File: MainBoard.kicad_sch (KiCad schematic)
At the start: 48 parts, among them SW1 SW_Push, SW10 SW_Push, SW11 SW_Push, SW12 SW_Push, SW13 SW_Push, SW14 SW_Push, SW15 SW_Push, SW16 SW_Push, SW17 SW_Push, SW18 SW_Push, SW19 SW_Push, SW2 SW_Push, SW20 SW_Push, SW21 SW_Push, SW22 SW_Push, SW23 SW_Push, SW3 SW_Push, SW4 SW_Push, SW5 SW_Push, SW6 SW_Push, SW7 SW_Push, SW8 SW_Push, SW9 SW_Push

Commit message: added PCB connectors
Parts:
- removed BZ1, BZ2: Buzzer, symbol Device:Buzzer
- removed D1, D10, D11, D2, D6, D7, D8, D9, docD5: LED, symbol Device:LED
- removed RV1, RV2: R_Potentiometer, symbol Device:R_Potentiometer
- removed SW1, SW11, SW12, SW13, SW14, SW15, SW16, SW17, SW2, SW3, SW4, SW5, SW6, SW7: SW_Push, symbol Switch:SW_Push
- added J1, J17, J18, J19: (no value), symbol higo:Z209BM_C_04_00_0000
- added J10, J23: (no value), symbol JST_JWPF:B03B-JWPF-SK-R
- added J11, J22: (no value), symbol JST_JWPF:B04B-JWPF-SK-R
- added J12: Conn_01x02, symbol Connector_Generic:Conn_01x02
- added J13: Conn_01x06, symbol Connector_Generic:Conn_01x06
- added J14, J16: Conn_01x09, symbol Connector_Generic:Conn_01x09
- added J2, J20: (no value), symbol higo:Z309BM_C_04_00_0000
- added J21: (no value), symbol JST_JWPF:B05B-JWPF-SK-R
- added J3: (no value), symbol higo:Z409BM_C_04_00_0000
- added J5: (no value), symbol higo:Z509BM_C_04_00_0000
- added J6: (no value), symbol higo:Z609BM_C_04_00_0000
- added J8: (no value), symbol higo:Z809FM_C_04_00_0000
- added J9: (no value), symbol JST_JWPF:B02B-JWPF-SK-R
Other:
- note added: "PAS"
- note added: "accelerator"
- note added: "brake left"
- note added: "brake right"
- note added: "front connector"
- note added: "left side blinker"
- note added: "lightning commodo"
- note added: "motor commodo"
- note added: "right side blinker"
- note added: "seat switch"
- note added: "tail connector"
- note added: "torque"
- note added: "trunk light"
- note added: "trunk switch"
- note removed: "7 Output Digital Rear 7 analog input Rear 6/7 Output Digital Front 6/7 analog input Front 5 analog IN HMI 20 digital input 4 digital output"
- note removed: "Assist + Assist - Reverse Forward speed limiter setpoint warning on/off ? GND"
- note removed: "Beware, different GND..."
- note removed: "Blinker Left Blinker Left Sequential Reverse light VCC T2 Brake T2 Fog light Blinker Right Blinker Right Sequential GND"
- note removed: "Blinker Left Side Light Left VCC E6C SW+ E6C SW- E6C Side Light Right Blinker Right Horn GND"
- note removed: "BrightstarTW A1 Vcc Blink GND"
- note removed: "BrightstarTW E6C Vcc (DRL) SW (shorting the sw SW wire switch between GND the mode DRL -> PASSING <-> DRIVING )"
- note removed: "BrightstarTW T2 Vcc (license plate + Pos) brake Vcc GND"
- note removed: "DK370"
- note removed: "PAS Front"
- note removed: "Speed limiter -> Mode switch, Assist <-> Speed limtier ?"
- note removed: "Throttle"
- note removed: "Torque rear"
- note removed: "VCC GND S1 S2 Torque"
- note removed: "VDS blinker + beam tell tale"
- note removed: "beam horn blinker L blinker R GND"
- note removed: "bonus for speed limiter"
- note removed: "https://ebikes.ca/resources/theory/pedal-assist.html"
- note removed: "left brake"
- note removed: "pedal regen"
- note removed: "right brake"
- note removed: "seat sensor"

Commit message: added output driver
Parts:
- removed SW10, SW18, SW19, SW20, SW21, SW22, SW23, SW8, SW9: SW_Push, symbol Switch:SW_Push
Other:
- sheet FrontLightsControl renamed outputdriver
- sheet HumanInterfaceCircuits renamed inputHMI
- removed sheet BMSinterface
- removed sheet BackLightsControl
- added sheet IMU (USB_PD.kicad_sch)
- sheet outputdriver ports: added Load0, Load1, Load10, Load11, Load12, Load13, Load14, Load15, Load16, Load17, Load18, Load19, Load2, Load3, Load4, Load5, Load6, Load7, Load8, Load9; removed none
- note added: "DONT FORGET : IMU foglight feedback buzzer"
- note added: "tell tale VDS"
- moved on the sheet: FID1, FID2, FID3, FID4, FID5, FID6, H1, H2, H3, H4, H5, H6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

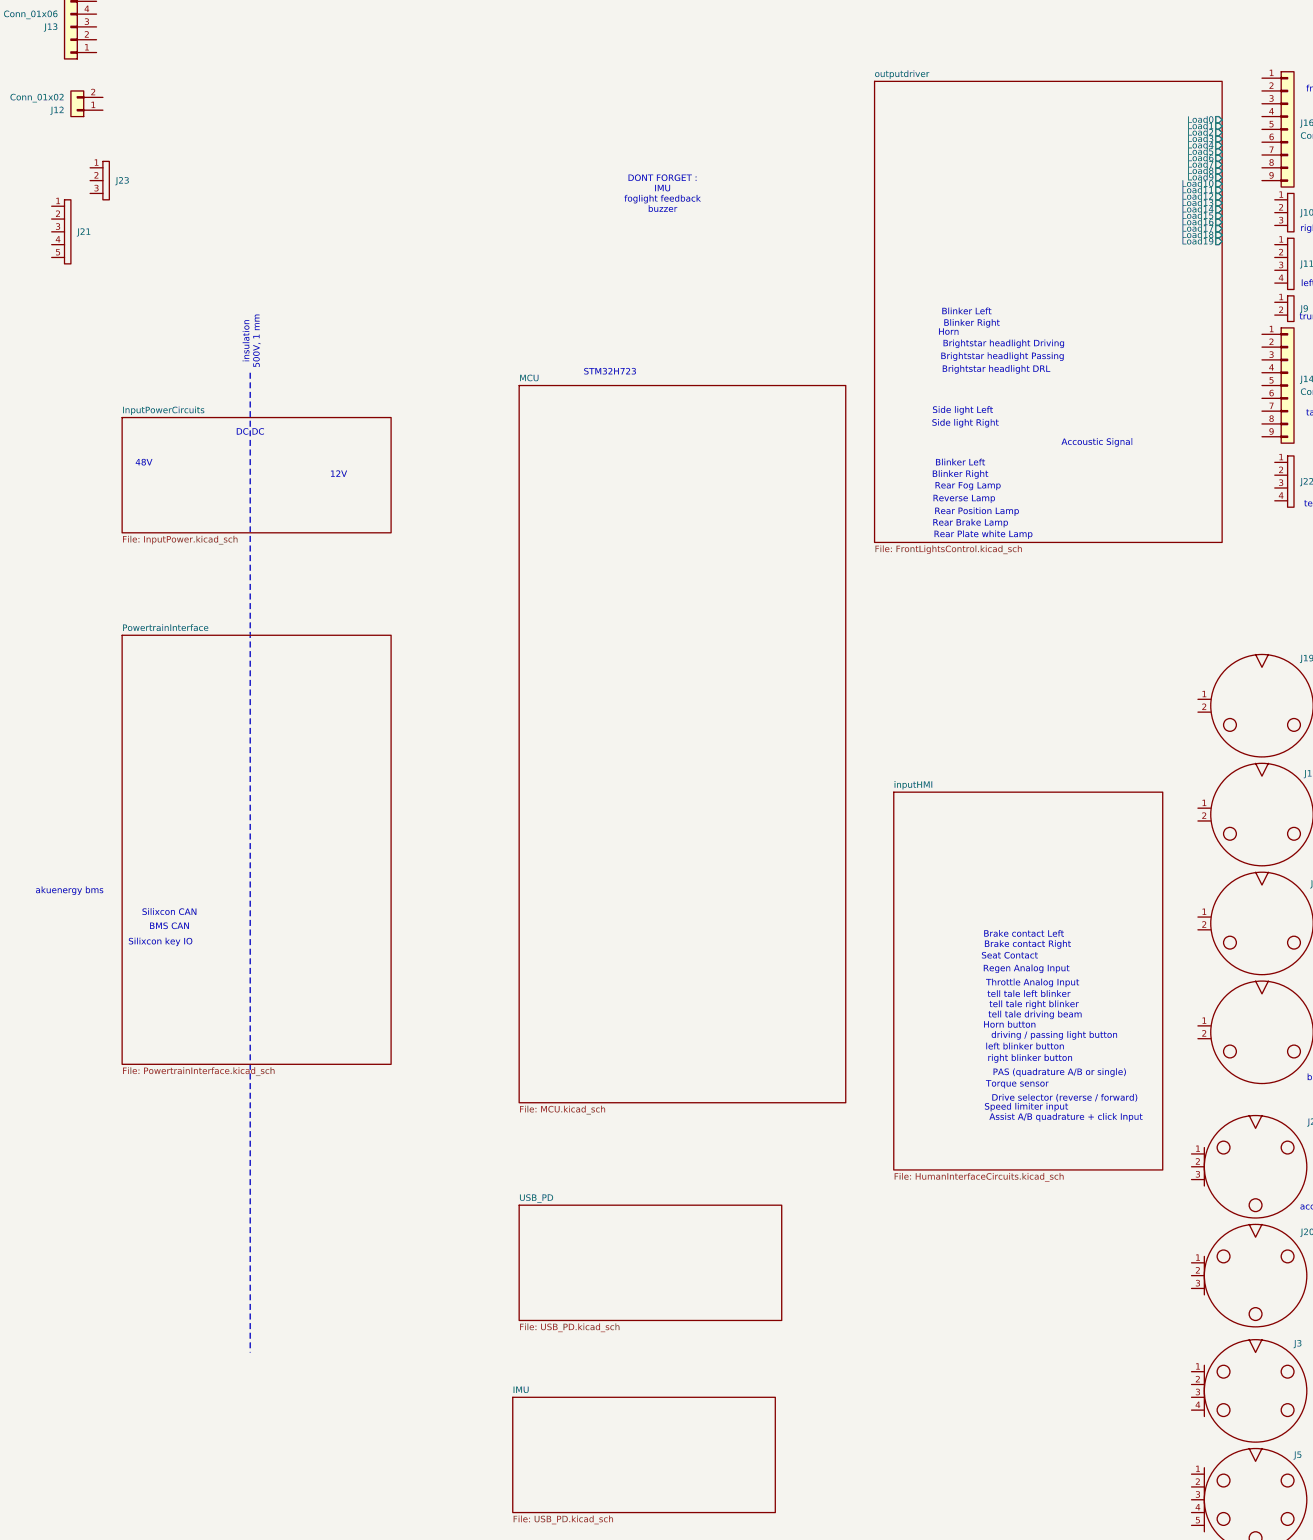
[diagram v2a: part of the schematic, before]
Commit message: added schematic for input (switch, PAS, analog) + output
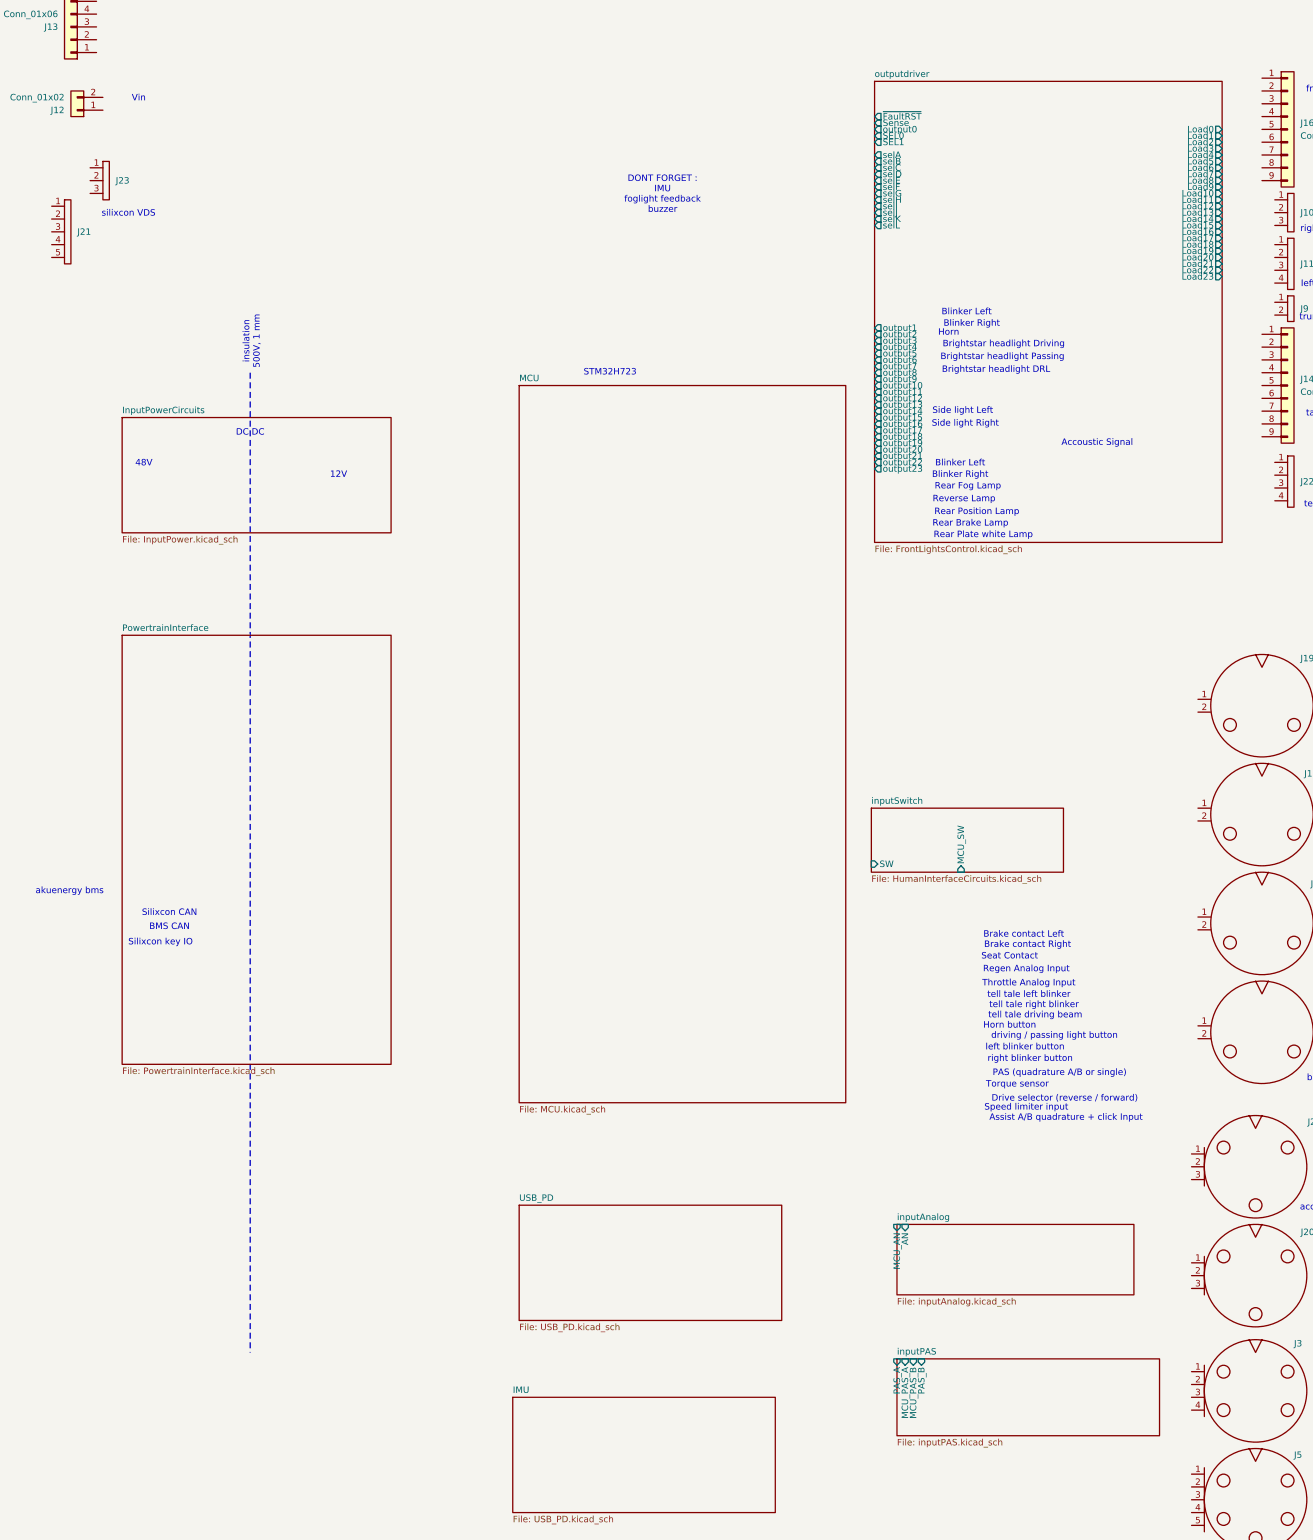
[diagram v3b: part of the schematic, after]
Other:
- sheet inputHMI renamed inputSwitch
- added sheet inputAnalog (inputAnalog.kicad_sch)
- added sheet inputPAS (inputPAS.kicad_sch)
- sheet inputSwitch ports: added MCU_SW, SW; removed none
- sheet outputdriver ports: added Load20, Load21, Load22, Load23, SEL0, SEL1, Sense, output0, output1, output10, output11, output12, output13, output14, output15, output16, output17, output18, output19, output2, output20, output21, output22, output23, output3, output4, output5, output6, output7, output8, output9, selA, selB, selC, selD, selE, selF, selG, selH, selI, selJ, selK, selL, ~{FaultRST}; removed none
- note added: "Vin"
- note added: "silixcon VDS"

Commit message: wiring MCU to input and ouput
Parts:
- added J25: (no value), symbol higo:Z609BM_C_04_00_0000
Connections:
- net inputAnalog/AN: now also J20.3
- net inputPAS/PAS_A: now also J6.4
- net inputPAS/PAS_B: now also J6.3
- net inputSwitch/SW: now also J19.2
- net outputdriver/Load0: now also J16.2 (Pin_2)
- net outputdriver/Load1: now also J16.3 (Pin_3)
- net outputdriver/Load10: now also J11.2
- net outputdriver/Load11: now also J11.3
- net outputdriver/Load12: now also J9.2
- net outputdriver/Load13: now also J14.2 (Pin_2)
- net outputdriver/Load14: now also J14.3 (Pin_3)
- net outputdriver/Load15: now also J14.4 (Pin_4)
- net outputdriver/Load16: now also J14.5 (Pin_5)
- net outputdriver/Load17: now also J14.6 (Pin_6)
- net outputdriver/Load18: now also J14.7 (Pin_7)
- net outputdriver/Load19: now also J14.8 (Pin_8)
- net outputdriver/Load2: now also J16.4 (Pin_4)
- net outputdriver/Load20: now also J14.9 (Pin_9)
- net outputdriver/Load21: now also J22.1
- net outputdriver/Load22: now also J22.2
- net outputdriver/Load23: now also J22.3
- net outputdriver/Load3: now also J16.5 (Pin_5)
- net outputdriver/Load4: now also J16.6 (Pin_6)
- net outputdriver/Load5: now also J16.7 (Pin_7)
- net outputdriver/Load6: now also J16.8 (Pin_8)
- net outputdriver/Load7: now also J16.9 (Pin_9)
- net outputdriver/Load8: now also J10.2
- net outputdriver/Load9: now also J10.3
- net GND: now reaches J5.1
- net GND: now also J1.1, J10.1, J11.1, J14.1 (Pin_1), J16.1 (Pin_1), J17.1, J18.1, J19.1, J2.2, J20.2, J22.4, J3.2, J6.2, J8.1, J9.1, J25.2
- net inputSwitch4/SW: now reaches J5.2
- net inputSwitch5/SW: now reaches J5.3
- net inputSwitch6/SW: now reaches J5.4
- net inputSwitch7/SW: now reaches J5.5
- net inputSwitch2/SW: now reaches J17.2
- net +5V: now reaches J2.1
- net +5V: now also J20.1, J3.1
- net inputAnalog2/AN: now reaches J2.3
- net inputSwitch3/SW: now reaches J1.2
- net +12V: now reaches J6.1
- net +12V: now also J25.1
- net inputAnalog1/AN: now reaches J6.5
- net inputPAS1/PAS_A: now reaches J3.3
- net inputPAS1/PAS_B: now reaches J3.4
- net inputSwitch1/SW: now reaches J18.2
- net inputSwitch8/SW: now reaches J8.2
- net inputSwitch9/SW: now reaches J8.3
- net inputSwitch10/SW: now reaches J8.4
- net inputSwitch11/SW: now reaches J8.5
- net inputSwitch12/SW: now reaches J8.6
- net inputSwitch13/SW: now reaches J8.7
- net inputSwitch14/SW: now reaches J8.8
- new net inputAnalog4/AN: J25.5
- new net inputPAS3/PAS_A: J25.4
- new net inputPAS3/PAS_B: J25.3
- no-connect marks 0 -> 3
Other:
- added sheet inputAnalog1 (inputAnalog.kicad_sch)
- added sheet inputAnalog2 (inputAnalog.kicad_sch)
- added sheet inputAnalog3 (inputAnalog.kicad_sch)
- added sheet inputAnalog4 (inputAnalog.kicad_sch)
- added sheet inputPAS1 (inputPAS.kicad_sch)
- added sheet inputPAS2 (inputPAS.kicad_sch)
- added sheet inputPAS3 (inputPAS.kicad_sch)
- added sheet inputSwitch1 (inputSwitch.kicad_sch)
- added sheet inputSwitch10 (inputSwitch.kicad_sch)
- added sheet inputSwitch11 (inputSwitch.kicad_sch)
- added sheet inputSwitch12 (inputSwitch.kicad_sch)
- added sheet inputSwitch13 (inputSwitch.kicad_sch)
- added sheet inputSwitch14 (inputSwitch.kicad_sch)
- added sheet inputSwitch2 (inputSwitch.kicad_sch)
- added sheet inputSwitch3 (inputSwitch.kicad_sch)
- added sheet inputSwitch4 (inputSwitch.kicad_sch)
- added sheet inputSwitch5 (inputSwitch.kicad_sch)
- added sheet inputSwitch6 (inputSwitch.kicad_sch)
- added sheet inputSwitch7 (inputSwitch.kicad_sch)
- added sheet inputSwitch8 (inputSwitch.kicad_sch)
- added sheet inputSwitch9 (inputSwitch.kicad_sch)
- sheet MCU ports: added PA0, PA1, PA15, PA2, PA3, PA4, PA5, PA6, PA7, PA8, PB0, PB1, PB12, PB13, PB14, PB15, PB2, PB3, PB4, PB5, PB6, PB7, PB8, PB9, PC0, PC1, PC10, PC11, PC12, PC13, PC2, PC3, PC4, PC5, PC6, PC7, PC8, PC9; removed none
- sheet inputSwitch: file HumanInterfaceCircuits.kicad_sch -> inputSwitch.kicad_sch
- note added: "Ground Front position lamp Front direction-indicator lamp, right Front direction-indicator lamp, left Passing-beam headlamp Driving-beam headlamp Daytime running lamp Audible warning device NA"
- note added: "Ground Rear direction-indicator lamp, right Rear direction-indicator lamp, left Stop lamp Rear position lamp Rear fog lamp Reversing lamp NA NA"
- note added: "HIGO MINI B - PIN NUMBERING BY WIRE COLOUR (Velion convention) Order: 1 RED, 2 BLACK, 3 YELLOW, 4 GREEN, 5 BLUE, 6 WHITE (skip colours the cable does not have; colour is the reference) 2 PIN: 1 BLK 2 WHT 3 PIN: 1 RED 2 BLK 3 WHT 4 PIN: 1 RED 2 BLK 3 YEL 4 GRN 5 PIN: 1 RED 2 BLK 3 YEL 4 GRN 5 BLU 6 PIN: 1 RED 2 BLK 3 YEL 4 GRN 5 BLU 6 WHT(centre) THROTTLE 390X/376ZX (3P Z309BG) 1 RED +5V 2 BLK GND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"
- note added: "Side direction-indicator lamp, left"
- note added: "Side direction-indicator lamp, right"
- note added: "Side-marker lamp, left"
- note added: "Side-marker lamp, right"
- note added: "Tell-tale Driving-beam"
- note added: "Tell-tale direction-indicator left"
- note added: "Tell-tale direction-indicator right"
- note added: "aux"
- note added: "cargo compartment lamp"
- note added: "drive commodo"
- note removed: "Accoustic Signal"
- note removed: "Blinker Left"
- note removed: "Blinker Right"
- note removed: "Brightstar headlight DRL"
- note removed: "Brightstar headlight Driving"
- note removed: "Brightstar headlight Passing"
- note removed: "Horn"
- note removed: "Rear Brake Lamp"
- note removed: "Rear Fog Lamp"
- note removed: "Rear Plate white Lamp"
- note removed: "Rear Position Lamp"
- note removed: "Reverse Lamp"
- note removed: "Side light Left"
- note removed: "Side light Right"
- note removed: "left side blinker"
- note removed: "motor commodo"
- note removed: "right side blinker"
- note removed: "tell tale VDS"
- note removed: "trunk light"
- moved on the sheet: J1, J10, J11, J14, J16, J17, J18, J19, J2, J20, J22, J3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

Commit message: started pin assignement
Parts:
- renumbered J21 to J1, J22 to J10, J19 to J11, J18 to J12, J17 to J13, J1 to J14, J2 to J15, J20 to J16, J3 to J17, J5 to J18, J6 to J19, J13 to J2, J25 to J20, J8 to J21, J12 to J3, J23 to J4, J16 to J5, J10 to J6, J11 to J7, J9 to J8, J14 to J9
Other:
- removed sheet inputAnalog3
- removed sheet inputPAS2
- sheet MCU ports: added PD0, PD1, PD10, PD11, PD12, PD13, PD14, PD15, PD2, PD3, PD4, PD5, PD6, PD7, PD8, PD9, PE0, PE1, PE10, PE11, PE12, PE13, PE14, PE15, PE2, PE3, PE4, PE5, PE6, PE7, PE8, PE9, PF0, PF1, PF10, PF11, PF12, PF13, PF14, PF15, PF2, PF3, PF4, PF5, PF6, PF7, PF8, PF9, PG0, PG1, PG10, PG11, PG12, PG13, PG14, PG15, PG2, PG3, PG4, PG5, PG6, PG7, PG8, PG9; removed none

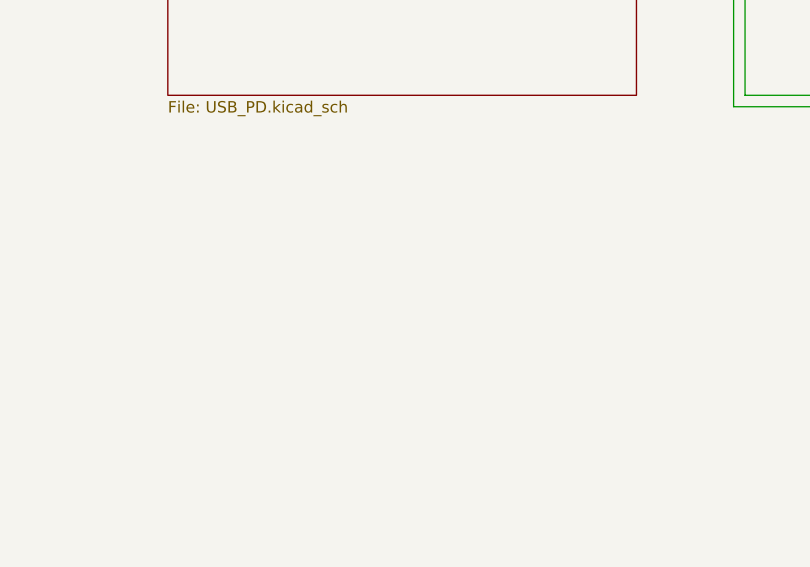
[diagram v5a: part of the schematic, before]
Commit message: added buzzer sheet
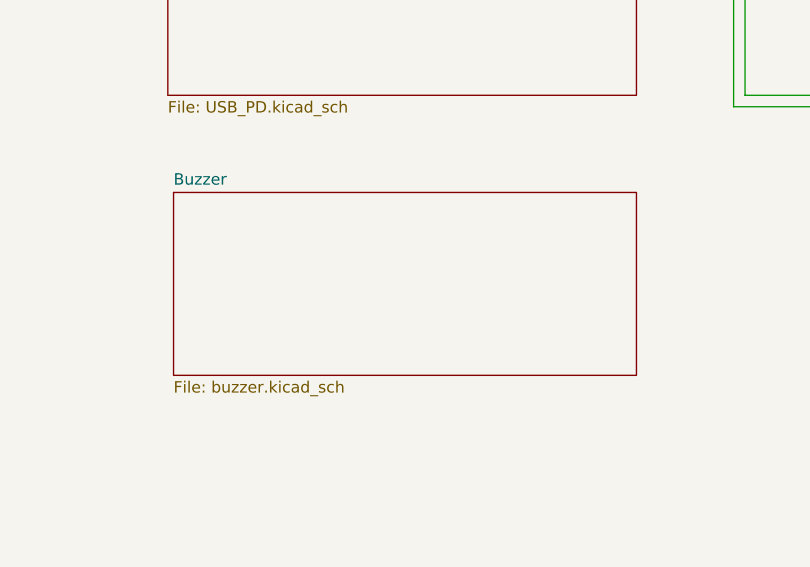
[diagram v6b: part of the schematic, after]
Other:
- added sheet Buzzer (buzzer.kicad_sch)
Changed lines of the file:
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@@
+	)
+	(sheet
+		(at 88.9 328.295)
+		(size 51.435 20.32)
+		(exclude_from_sim no)
+		(in_bom yes)
+		(on_board yes)
+		(dnp no)
+		(fields_autoplaced yes)
+		(stroke
+			(width 0.1524)
+			(type solid)
+		)
+		(fill
+			(color 0 0 0 0)
+		)
+		(property "Sheetname" "Buzzer"
+			(at 88.9 327.5834 0)
+			(show_name no)
+			(do_not_autoplace no)
+			(effects
+				(font
+					(size 1.27 1.27)
+				)
+				(justify left bottom)
+			)
+		)
+		(property "Sheetfile" "buzzer.kicad_sch"
+			(at 88.9 349.1996 0)
+			(show_name no)
+			(do_not_autoplace no)
+			(effects
+				(font
+					(size 1.27 1.27)
+				)
+				(justify left top)
+			)
+		)
+		(instances
+			(project "MainBoard"
+				(path "/6deb7572-40fc-4be3-9f80-b7a356c09b38"
+					(page "28")
+				)
+			)
+		)
 	)
 	(sheet
